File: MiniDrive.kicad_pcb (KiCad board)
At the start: 2 copper layers, 25 x 39.5 mm, 20 parts, among them J1 Conn_LED, J2 Conn_24V, U1 TPS92200

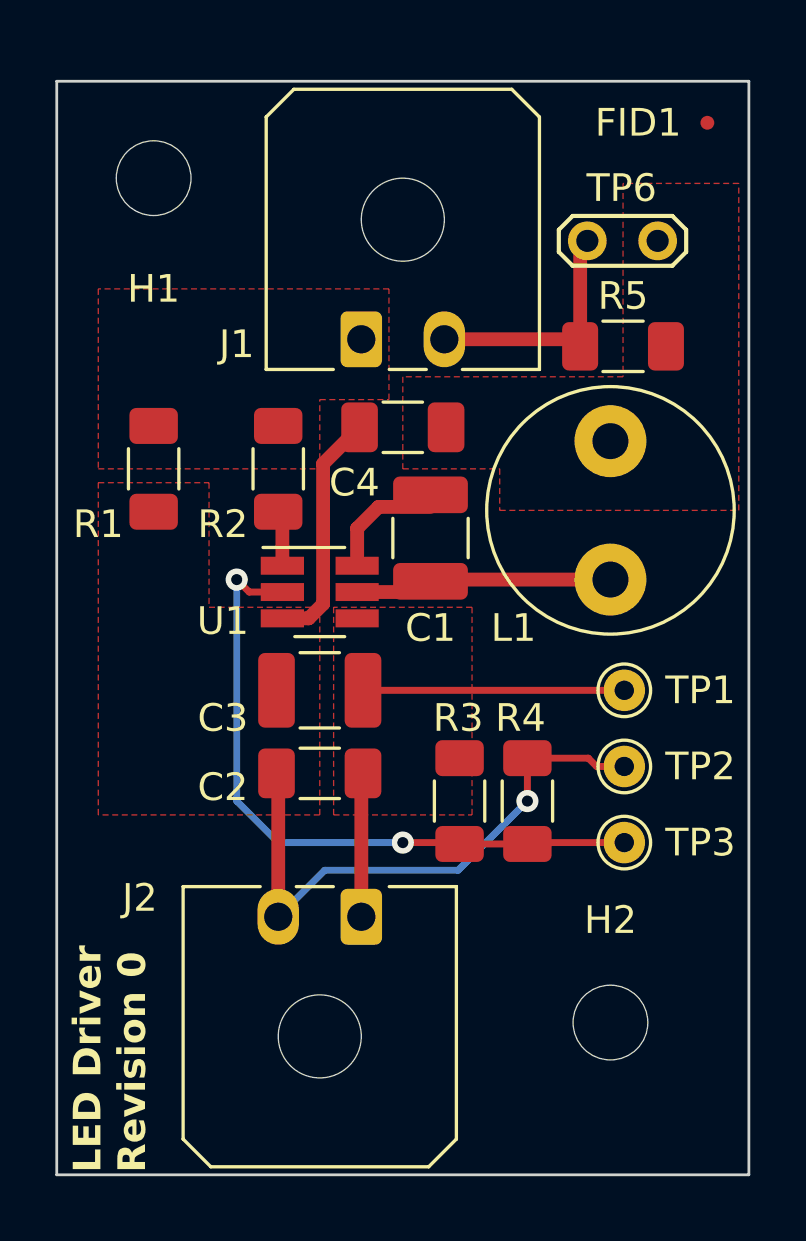
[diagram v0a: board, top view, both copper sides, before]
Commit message: Minor layout improvements
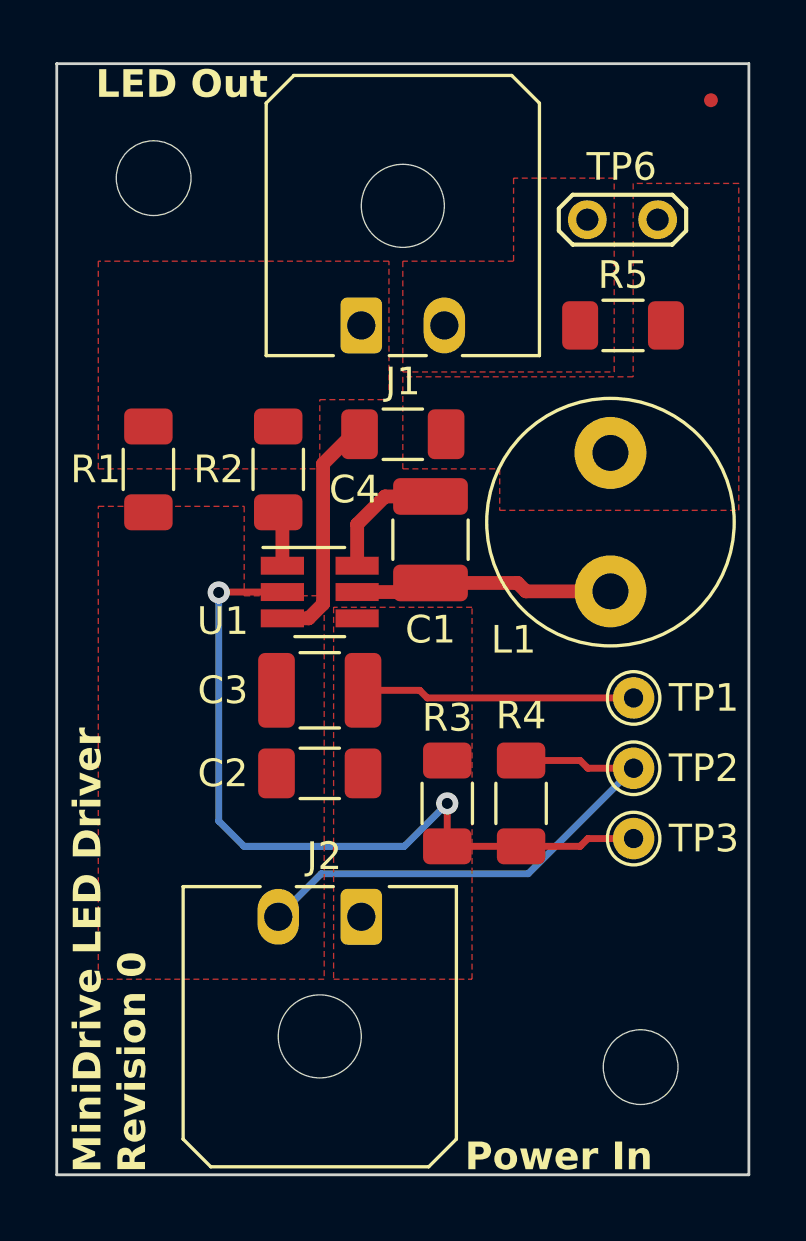
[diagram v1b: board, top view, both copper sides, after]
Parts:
- moved H2 1.94 mm to (148.6, 118.1)
- moved FID1 0.83 mm to (151.1, 83.2)
- moved TP6 0.77 mm to (149.2, 87.5)
- moved R5 0.76 mm to (148.0, 91.3)
- moved J1 0.50 mm to (138.5, 91.3)
- moved R3 0.45 mm to (141.6, 108.6)
- moved TP1 0.43 mm to (148.3, 104.8)
- moved L1 0.42 mm to (147.5, 100.9)
- moved TP3 0.37 mm to (148.3, 109.9)
- moved TP2 0.34 mm to (148.3, 107.3)
- moved C4 0.25 mm to (140.0, 95.2)
- moved R4 0.24 mm to (144.3, 108.6)
- moved R1 0.19 mm to (130.8, 96.5)
- moved C1 0.06 mm to (141.0, 99.1)
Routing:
- net Net-(J1-Pin_2): track 8.93 -> 0.00 mm
- net +24V: track 14.7 -> 9.96 mm
- net Net-(U1-DIM): track 24.5 -> 28.2 mm
- net GND: track 29.7 -> 27.8 mm, vias 1 -> 0
- net Net-(U1-SW): track 9.34 -> 9.96 mm
- added copper zone on F.Cu, net Net-(J1-Pin_2)
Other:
- board size 25 x 39.5 mm -> 25 x 40.1 mm
- board text added: "LED Out"
- board text added: "MiniDrive LED Driver Revision 0"
- board text added: "Power In"
- board text removed: "LED Driver Revision 0"

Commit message: Add C5 to layout
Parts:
- added C5: 0.1uF, Capacitor_SMD:C_0402_1005Metric_Pad0.74x0.62mm_HandSolder, F.Cu at (133.3, 99.7)
- added TP4: TestPoint, TestPoint:TestPoint_THTPad_D1.5mm_Drill0.7mm, F.Cu at (131.4, 92.1)
- TP1: value TestPoint -> +24V
- TP2: value TestPoint -> GND
- TP3: value TestPoint -> V_DIM
- TP5: renamed from TP6; value TestPoint_2Pole -> Current Meter
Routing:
- net Net-(U1-FB): track 2.01 -> 3.66 mm
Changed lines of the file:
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@@
         (effects (font (size 1 1) (thickness 0.15)))
     )
-    (fp_text value "TestPoint" (at 0 1.75) (layer "F.Fab") hide
+    (fp_text value "+24V" (at 0 1.75) (layer "F.Fab") hide
         (effects (font (size 1 1) (thickness 0.15)))
     )
@@
     (property "ki_keywords" "point tp")
     (attr exclude_from_pos_files)
-    (fp_text reference "TP6" (at 1.3 1.905) (layer "F.SilkS")
-        (effects (font (size 1 1) (thickness 0.15)))
-    )
-    (fp_text value "TestPoint_2Pole" (at 1.27 2) (layer "F.Fab") hide
+    (fp_text reference "TP5" (at 1.3 1.905) (layer "F.SilkS")
+        (effects (font (size 1 1) (thickness 0.15)))
+    )
+    (fp_text value "Current Meter" (at 1.27 2) (layer "F.Fab") hide
         (effects (font (size 1 1) (thickness 0.15)))
     )
@@
     )
   )
+  (footprint "Capacitor_SMD:C_0402_1005Metric_Pad0.74x0.62mm_HandSolder" (layer "F.Cu")
+    (at 133.35 99.695 180)
+    (descr "Capacitor SMD 0402 (1005 Metric), square (rectangular) end terminal, IPC_7351 nominal with elongated pad for handsoldering. (Body size source: IPC-SM-782 page 76, https://www.pcb-3d.com/wordpress/wp-content/uploads/ipc-sm-782a_amendment_1_and_2.pdf), generated with kicad-footprint-generator")
+    (tags "capacitor handsolder")
+    (property "Sheetfile" "MiniDrive.kicad_sch")
+    (property "Sheetname" "")
+    (property "dnp" "")
+    (property "ki_description" "Unpolarized capacitor")
+    (property "ki_keywords" "cap capacitor")
+    (attr smd)
+    (fp_text reference "C5" (at 0 -1.16) (layer "F.SilkS")
+        (effects (font (size 1 1) (thickness 0.15)))
+    )
+    (fp_text value "0.1uF" (at 0 1.16) (layer "F.Fab")
+        (effects (font (size 1 1) (thickness 0.15)))
+    )
+    (fp_text user "${REFERENCE}" (at 0 0) (layer "F.Fab")
+        (effects (font (size 0.25 0.25) (thickness 0.04)))
+    )
+    (fp_line (start -0.115835 -0.36) (end 0.115835 -0.36)
+      (stroke (width 0.12) (type solid)) (layer "F.SilkS"))
+    (fp_line (start -0.115835 0.36) (end 0.115835 0.36)
+      (stroke (width 0.12) (type solid)) (layer "F.SilkS"))
+    (fp_line (start -1.08 -0.46) (end 1.08 -0.46)
+      (stroke (width 0.05) (type solid)) (layer "F.CrtYd"))
+    (fp_line (start -1.08 0.46) (end -1.08 -0.46)
+      (stroke (width 0.05) (type solid)) (layer "F.CrtYd"))
+    (fp_line (start 1.08 -0.46) (end 1.08 0.46)
+      (stroke (width 0.05) (type solid)) (layer "F.CrtYd"))
+    (fp_line (start 1.08 0.46) (end -1.08 0.46)
+      (stroke (width 0.05) (type solid)) (layer "F.CrtYd"))
+    (fp_line (start -0.5 -0.25) (end 0.5 -0.25)
+      (stroke (width 0.1) (type solid)) (layer "F.Fab"))
+    (fp_line (start -0.5 0.25) (end -0.5 -0.25)
+      (stroke (width 0.1) (type solid)) (layer "F.Fab"))
+    (fp_line (start 0.5 -0.25) (end 0.5 0.25)
+      (stroke (width 0.1) (type solid)) (layer "F.Fab"))
+    (fp_line (start 0.5 0.25) (end -0.5 0.25)
+      (stroke (width 0.1) (type solid)) (layer "F.Fab"))
+    (pad "1" smd roundrect (at -0.5675 0 180) (size 0.735 0.62) (layers "F.Cu" "F.Paste" "F.Mask") (roundrect_rratio 0.25)
+      (net 7 "Net-(U1-FB)") (pintype "passive"))
+    (pad "2" smd roundrect (at 0.5675 0 180) (size 0.735 0.62) (layers "F.Cu" "F.Paste" "F.Mask") (roundrect_rratio 0.25)
+      (net 4 "GND") (pintype "passive"))
+    (model "${KICAD6_3DMODEL_DIR}/Capacitor_SMD.3dshapes/C_0402_1005Metric.wrl"
+      (offset (xyz 0 0 0))
+      (scale (xyz 1 1 1))
+      (rotate (xyz 0 0 0))
+    )
+  )
   (footprint "Resistor_SMD:R_1206_3216Metric_Pad1.30x1.75mm_HandSolder" (layer "F.Cu")
     (at 135.5 96.52 -90)
@@
         (effects (font (size 1 1) (thickness 0.15)))
     )
-    (fp_text value "TestPoint" (at 0 1.75) (layer "F.Fab") hide
+    (fp_text value "V_DIM" (at 0 1.75) (layer "F.Fab") hide
         (effects (font (size 1 1) (thickness 0.15)))
     )
@@
   )
   (footprint "TestPoint:TestPoint_THTPad_D1.5mm_Drill0.7mm" (layer "F.Cu")
+    (at 131.445 92.075)
+    (descr "THT pad as test Point, diameter 1.5mm, hole diameter 0.7mm")
+    (tags "test point THT pad")
+    (property "Sheetfile" "MiniDrive.kicad_sch")
+    (property "Sheetname" "")
+    (property "ki_description" "test point")
+    (property "ki_keywords" "test point tp")
+    (attr exclude_from_pos_files)
+    (fp_text reference "TP4" (at 0 -1.648) (layer "F.SilkS")
+        (effects (font (size 1 1) (thickness 0.15)))
+    )
+    (fp_text value "TestPoint" (at 0 1.75) (layer "F.Fab") hide
+        (effects (font (size 1 1) (thickness 0.15)))
+    )
+    (fp_text user "${REFERENCE}" (at 0 -1.65) (layer "F.Fab")
+        (effects (font (size 1 1) (thickness 0.15)))
+    )
+    (fp_circle (center 0 0) (end 0 0.95)
+      (stroke (width 0.12) (type solid)) (fill none) (layer "F.SilkS"))
+    (fp_circle (center 0 0) (end 1.25 0)
+      (stroke (width 0.05) (type solid)) (fill none) (layer "F.CrtYd"))
+    (pad "1" thru_hole circle (at 0 0) (size 1.5 1.5) (drill 0.7) (layers "*.Cu" "*.Mask")
+      (net 5 "Net-(J1-Pin_1)") (pinfunction "1") (pintype "passive"))
+  )
+  (footprint "TestPoint:TestPoint_THTPad_D1.5mm_Drill0.7mm" (layer "F.Cu")
     (at 148.336 107.315)
     (descr "THT pad as test Point, diameter 1.5mm, hole diameter 0.7mm")
@@
         (effects (font (size 1 1) (thickness 0.15)))
     )
-    (fp_text value "TestPoint" (at 0 1.75) (layer "F.Fab") hide
+    (fp_text value "GND" (at 0 1.75) (layer "F.Fab") hide
         (effects (font (size 1 1) (thickness 0.15)))
     )
@@
   (segment (start 144.526 111.125) (end 137.055 111.125) (width 0.25) (layer "B.Cu") (net 4))
   (segment (start 148.336 107.315) (end 144.526 111.125) (width 0.25) (layer "B.Cu") (net 4))
-  (segment (start 135.65 98.2) (end 135.5 98.05) (width 0.25) (layer "F.Cu") (net 7))
+  (segment (start 134.2225 100) (end 133.9175 99.695) (width 0.5) (layer "F.Cu") (net 7))
   (segment (start 135.65 100) (end 135.65 98.2) (width 0.5) (layer "F.Cu") (net 7))
+  (segment (start 135.65 100) (end 134.2225 100) (width 0.5) (layer "F.Cu") (net 7))
   (segment (start 146.405 110.135) (end 144.272 110.135) (width 0.25) (layer "F.Cu") (net 8))
   (segment (start 141.605 110.135) (end 141.605 108.585) (width 0.25) (layer "F.Cu") (net 8))
@@
   )
   (zone (net 4) (net_name "GND") (layer "F.Cu") (hatch edge 0.5)
-    (connect_pads (clearance 0.5))
+    (connect_pads yes (clearance 0.5))
     (min_thickness 0.25) (filled_areas_thickness no)
     (fill yes (thermal_gap 0.5) (thermal_bridge_width 0.5))
